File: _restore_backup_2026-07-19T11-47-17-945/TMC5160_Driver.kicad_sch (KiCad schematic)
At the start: 36 parts, among them J9 BLR-514-5-V, Q21 MCM3400A-TP, Q22 MCM3400A-TP, Q23 MCM3400A-TP, Q24 MCM3400A-TP, U11 TMC5160A-TA-T

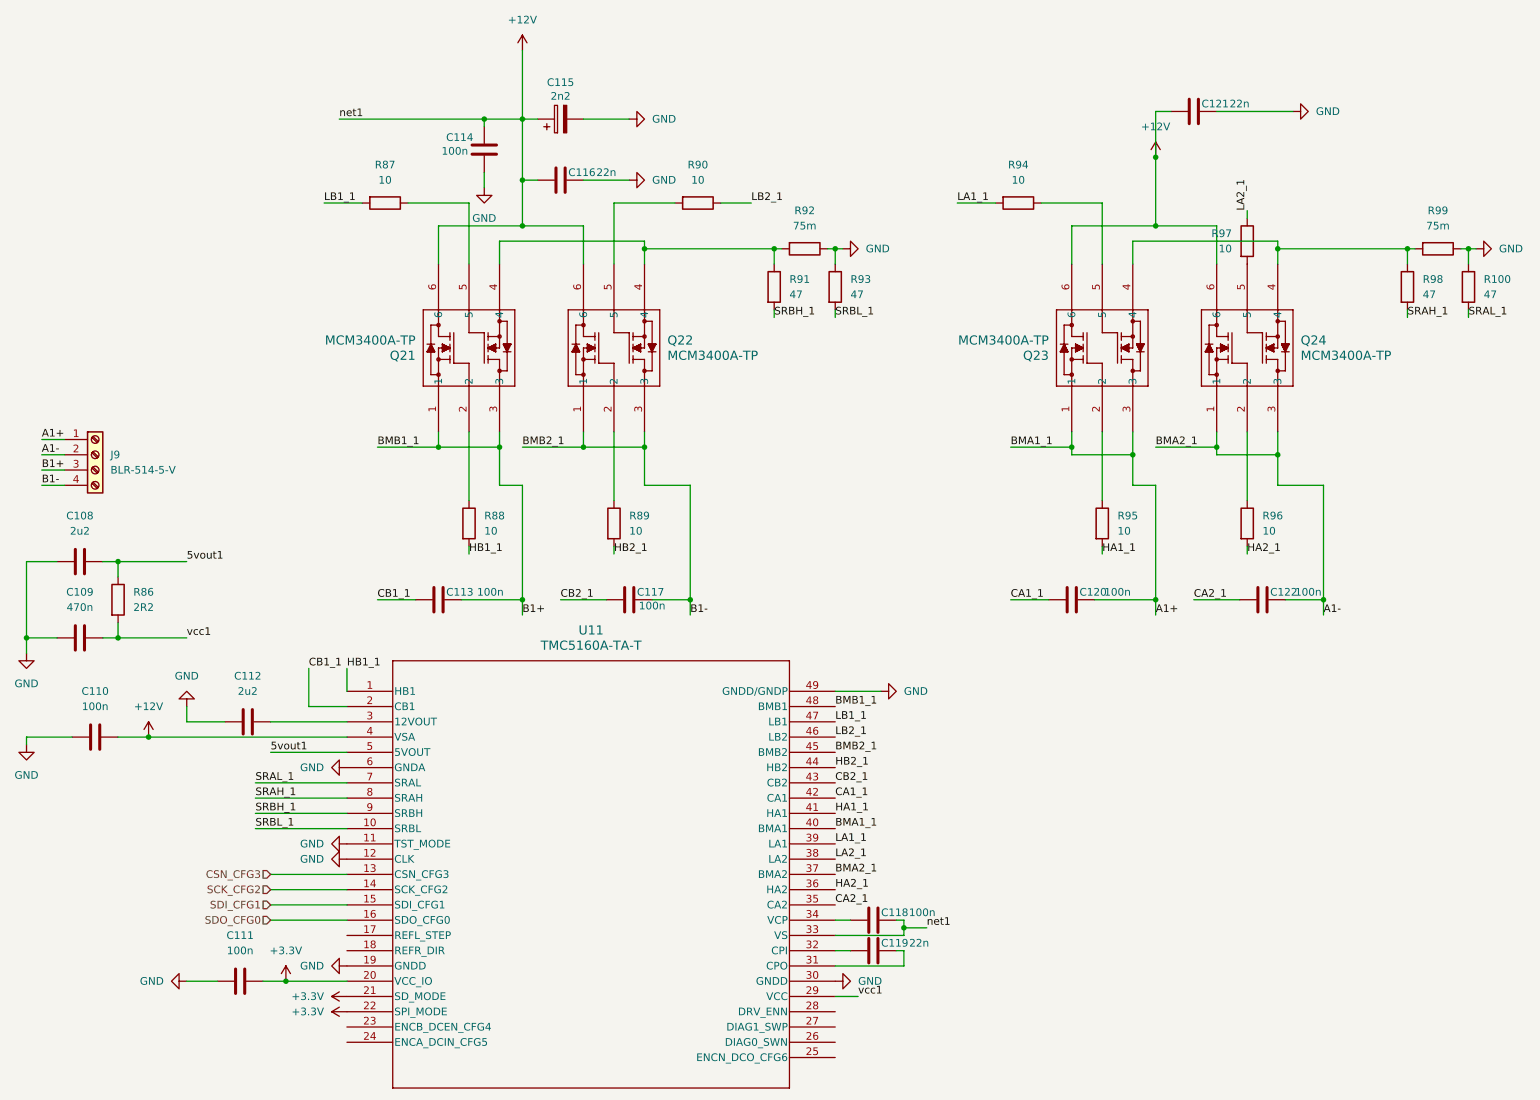
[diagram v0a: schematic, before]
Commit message: Updated Footprints for PCB. Started footprint layout and trace routing
Signed-off-by: Vincent Cadicamo <vcadicamo@icloud.com>
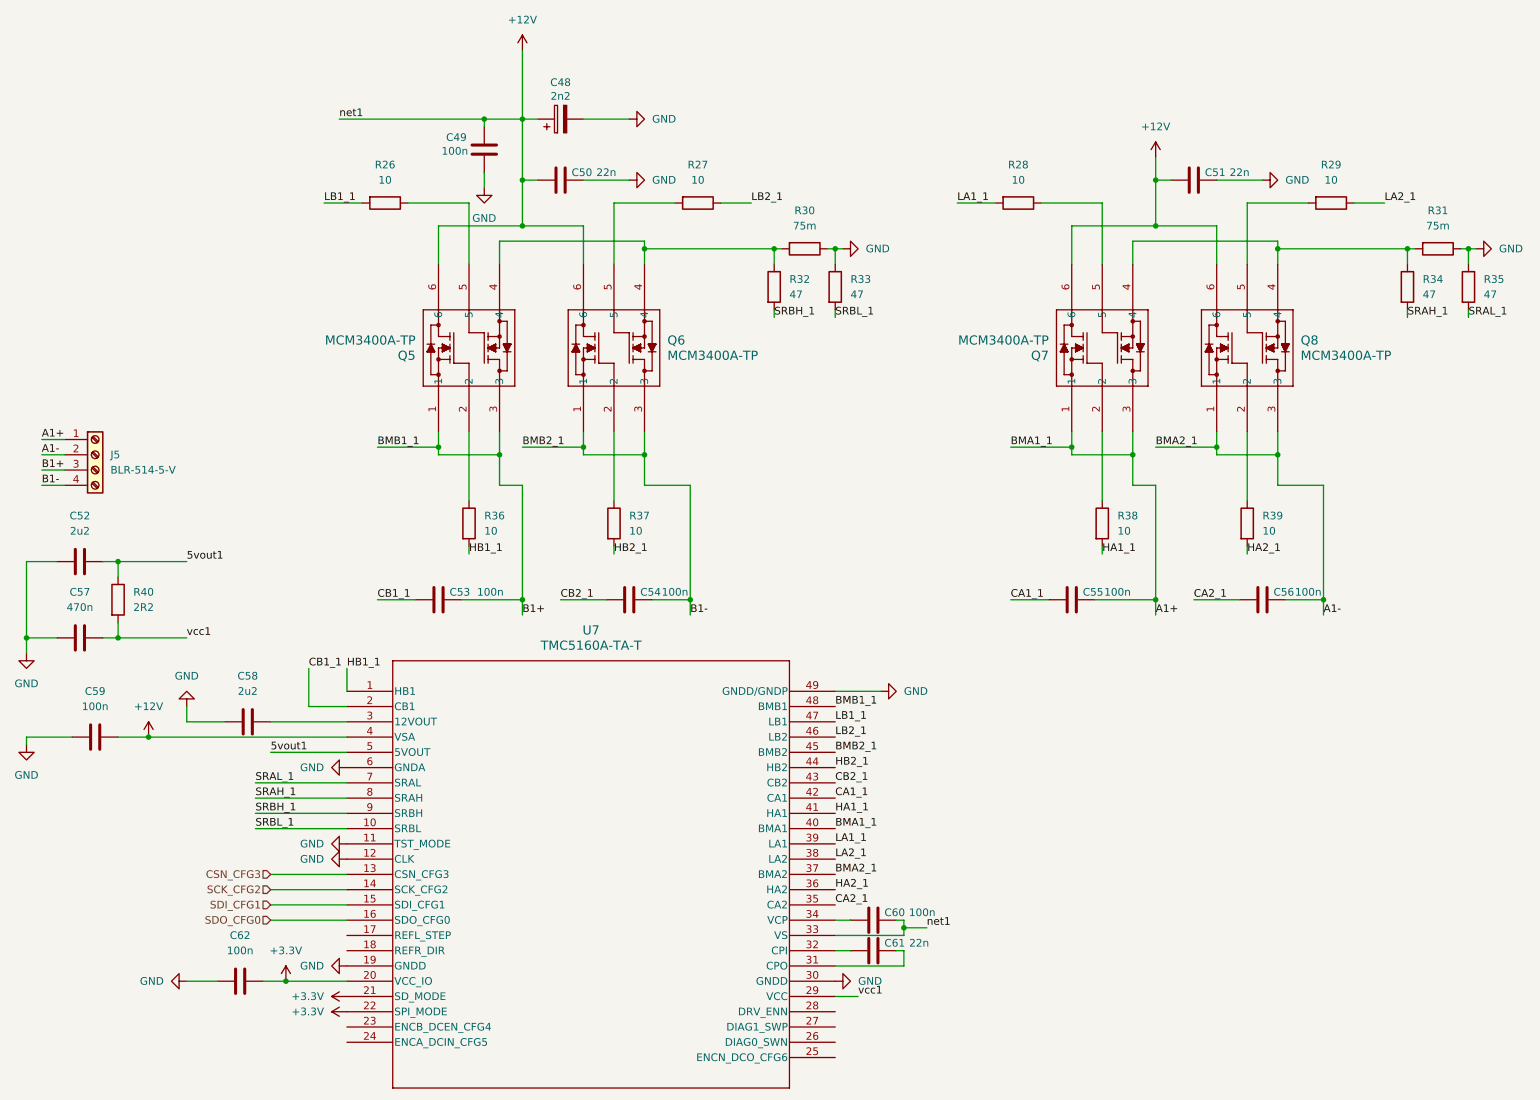
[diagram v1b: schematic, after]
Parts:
- C48: renamed from C115; footprint Capacitor_THT:CP_Radial_D10.0mm_P5.00mm -> (none)
- J5: renamed from J9; footprint TerminalBlock_Dinkle:TerminalBlock_Dinkle_DT-55-B01X-04_P10.00mm -> (none)
- Q5: renamed from Q21; footprint Stepper_ESC:DFN2020-6L_MCE -> DFN2020-6L_MCE
- Q6: renamed from Q22; footprint Stepper_ESC:DFN2020-6L_MCE -> DFN2020-6L_MCE
- Q7: renamed from Q23; footprint Stepper_ESC:DFN2020-6L_MCE -> DFN2020-6L_MCE
- Q8: renamed from Q24; footprint Stepper_ESC:DFN2020-6L_MCE -> DFN2020-6L_MCE
- R26: renamed from R87; footprint Resistor_SMD:R_0402_1005Metric -> (none)
- R27: renamed from R90; footprint Resistor_SMD:R_0402_1005Metric -> (none)
- R28: renamed from R94; footprint Resistor_SMD:R_0402_1005Metric -> (none)
- R29: renamed from R97; footprint Resistor_SMD:R_0402_1005Metric -> (none)
- R30: renamed from R92; footprint Resistor_SMD:R_0402_1005Metric -> (none)
- R31: renamed from R99; footprint Resistor_SMD:R_0402_1005Metric -> (none)
- R32: renamed from R91; footprint Resistor_SMD:R_0402_1005Metric -> (none)
- R33: renamed from R93; footprint Resistor_SMD:R_0402_1005Metric -> (none)
- R34: renamed from R98; footprint Resistor_SMD:R_0402_1005Metric -> (none)
- R35: renamed from R100; footprint Resistor_SMD:R_0402_1005Metric -> (none)
- R36: renamed from R88; footprint Resistor_SMD:R_0402_1005Metric -> (none)
- R37: renamed from R89; footprint Resistor_SMD:R_0402_1005Metric -> (none)
- R38: renamed from R95; footprint Resistor_SMD:R_0402_1005Metric -> (none)
- R39: renamed from R96; footprint Resistor_SMD:R_0402_1005Metric -> (none)
- R40: renamed from R86; footprint Resistor_SMD:R_0402_1005Metric -> (none)
- U7: renamed from U11; footprint Stepper_ESC:21-100582_ADI -> 21-100582_ADI
- renumbered C114 to C49, C116 to C50, C121 to C51, C108 to C52, C113 to C53, C117 to C54, C120 to C55, C122 to C56, C109 to C57, C112 to C58, C110 to C59, C118 to C60, C119 to C61, C111 to C62
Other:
- moved on the sheet: C51, R29
